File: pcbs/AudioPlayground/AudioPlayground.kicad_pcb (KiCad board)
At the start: 6 copper layers, 69.7 x 22.9 mm, 144 parts, among them J1 Conn_01x07_Socket, J2 Conn_Battery, J3 USB_C_Receptacle_USB2.0_14P, J4 TC2030, J5 Conn_01x12_Pin, J7 Conn_01x16_Pin, J9 Conn_01x07_Socket, U1 nRF5340-QKxx, U10 MCP73831-2-OT, U11 SN74LVC1G66DRYR, U12 AP2280, U13 SN74LVC1G66DRYR, U14 TS3USB221ARSER, U15 USBLC6-2P6, U16 SN74LVC1G66DRYR, U17 SN74LVC1G66DRYR, U19 GTD3526BA-1N, U2 R7FA4M2AB3CNE, U20 GTD3526BA-1N, U21 SN74LVC1G66DRYR, U3 USB2422/MJ, U4 MAX9867, U5 XC6209F332MR, U6 XC6209F182MR, U7 DMM-4326-T-R, U8 DMM-4326-T-R, U9 LM66200DRLR, Y1 32MHz, Y2 12mHz, Y3 24MHz, Y4 32.768kHz

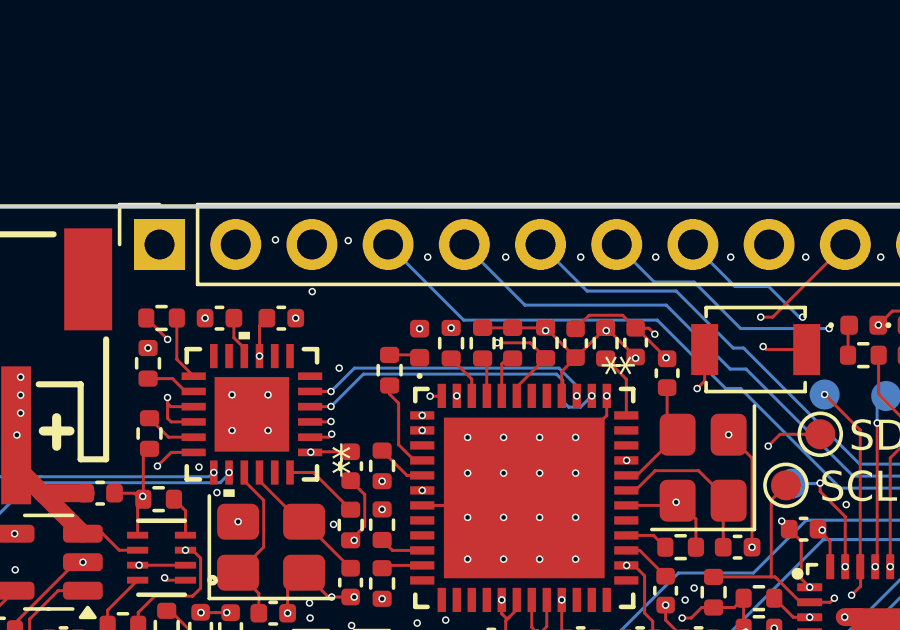
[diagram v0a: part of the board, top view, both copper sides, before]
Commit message: moved interface MCU LED to 3.3V switched
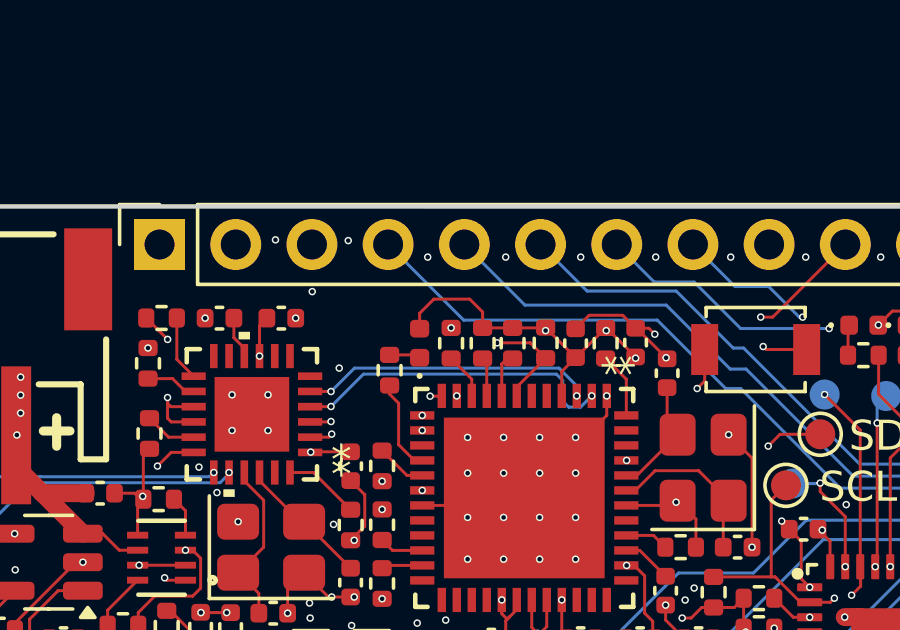
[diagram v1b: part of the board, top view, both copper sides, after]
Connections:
- D0 pad 2: +3.3V -> +3.3V_SWITCHED
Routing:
- net +3.3V_SWITCHED: track 141.3 -> 144.9 mm
- net +3.3V: vias 35 -> 34
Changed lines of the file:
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@@
 			(size 0.65 0.65)
 			(drill 0.65)
-			(layers "F&B.Cu" "*.Mask")
+			(layers "*.Cu" "*.Mask")
 		)
 		(pad "" np_thru_hole circle
@@
 			(size 0.65 0.65)
 			(drill 0.65)
-			(layers "F&B.Cu" "*.Mask")
+			(layers "*.Cu" "*.Mask")
 		)
 		(pad "A1" smd roundrect
@@
 			(layers "F.Cu" "F.Mask" "F.Paste")
 			(roundrect_rratio 0.25)
-			(net 6 "+3.3V")
+			(net 39 "+3.3V_SWITCHED")
 			(pinfunction "A")
 			(pintype "passive")
@@
 	)
 	(via
-		(at 120.148949 125.553949)
-		(size 0.25)
-		(drill 0.15)
-		(layers "F.Cu" "B.Cu")
-		(teardrops
-			(best_length_ratio 0.5)
-			(max_length 1)
-			(best_width_ratio 1)
-			(max_width 2)
-			(curved_edges yes)
-			(filter_ratio 0.9)
-			(enabled no)
-			(allow_two_segments yes)
-			(prefer_zone_connections yes)
-		)
-		(net 6)
-	)
-	(via
 		(at 116.967749 137.837949)
 		(size 0.25)
@@
 	)
 	(segment
+		(start 122.248949 124.998949)
+		(end 122.248949 125.528949)
+		(width 0.1)
+		(layer "F.Cu")
+		(net 39)
+	)
+	(segment
 		(start 124.358949 125.528949)
 		(end 125.348949 126.518949)
@@
 	)
 	(segment
+		(start 121.818949 124.568949)
+		(end 122.248949 124.998949)
+		(width 0.1)
+		(layer "F.Cu")
+		(net 39)
+	)
+	(segment
 		(start 127.038245 129.946098)
 		(end 127.048949 129.946098)
@@
 	)
 	(segment
+		(start 120.624467 124.568949)
+		(end 121.818949 124.568949)
+		(width 0.1)
+		(layer "F.Cu")
+		(net 39)
+	)
+	(segment
 		(start 120.253549 138.96895)
 		(end 119.609349 138.96895)
@@
 	)
 	(segment
+		(start 120.148949 125.044467)
+		(end 120.624467 124.568949)
+		(width 0.1)
+		(layer "F.Cu")
+		(net 39)
+	)
+	(segment
 		(start 117.551949 141.089149)
 		(end 116.739149 141.089149)
 		(width 0.1)
 		(layer "F.Cu")
+		(net 39)
+	)
+	(segment
+		(start 120.148949 125.553949)
+		(end 120.148949 125.044467)
+		(width 0.1)
+		(layer "F.Cu")

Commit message: Cleanup
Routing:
- net /IO/WING_EN: track 18.5 -> 18.0 mm
- net VBUS: vias 7 -> 6
- net GND: vias 245 -> 246

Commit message: V2.1
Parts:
- added TP10: TX, TestPoint:TestPoint_Pad_D1.0mm, B.Cu at (122.9, 136.8)
- added TP11: RX, TestPoint:TestPoint_Pad_D1.0mm, B.Cu at (122.9, 138.8)
- added TP8: SWDIO, TestPoint:TestPoint_Pad_D1.0mm, B.Cu at (153.1, 136.9)
- added TP9: SWDCLK, TestPoint:TestPoint_Pad_D1.0mm, B.Cu at (151.1, 136.9)
- moved G*** 8.63 mm to (136.5, 136.3)
- moved G*** 4.59 mm to (112.1, 131.0)
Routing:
- net /MCU/VCOM.TXD: track 41.3 -> 49.4 mm
- net /MCU/SWD.SWDIO: track 40.7 -> 46.0 mm
- net /MCU/VCOM.RXD: track 36.7 -> 40.8 mm
- net /MCU/SWD.SWDCLK: track 44.0 -> 45.4 mm

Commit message: Add Mounting Holes
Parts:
- added ?: , , F.Cu at (143.2, 123.4)
- added REF**: MountingHole_2.2mm_M2, MountingHole:MountingHole_2.2mm_M2, F.Cu at (143.2, 142.5)
- added REF**: MountingHole_2.2mm_M2, MountingHole:MountingHole_2.2mm_M2, F.Cu at (97.5, 124.1)
- added REF**: MountingHole_2.2mm_M2, MountingHole:MountingHole_2.2mm_M2, F.Cu at (143.2, 123.4)
- added REF**: MountingHole_2.2mm_M2, MountingHole:MountingHole_2.2mm_M2, F.Cu at (97.5, 141.8)
